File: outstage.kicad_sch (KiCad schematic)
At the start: 4 parts, among them M3001 Fan, M3002 Fan

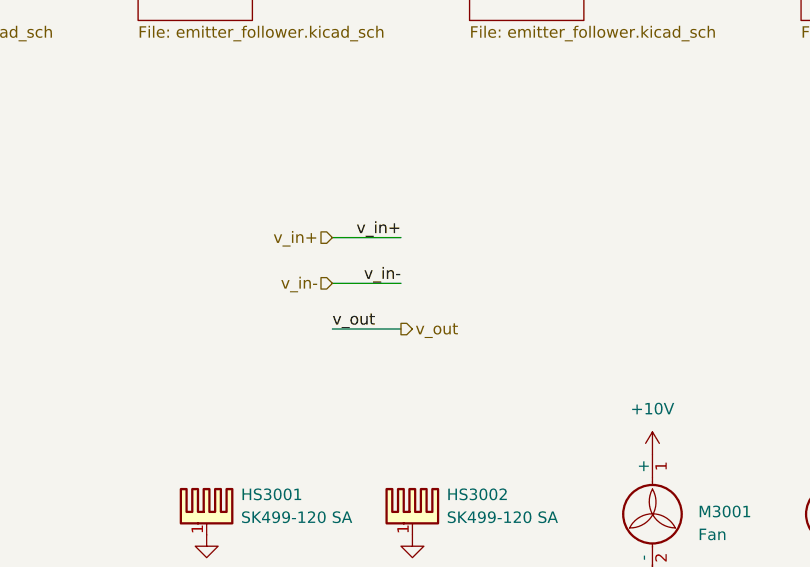
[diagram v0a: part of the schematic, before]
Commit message: add pss 3dmodels and testpoints
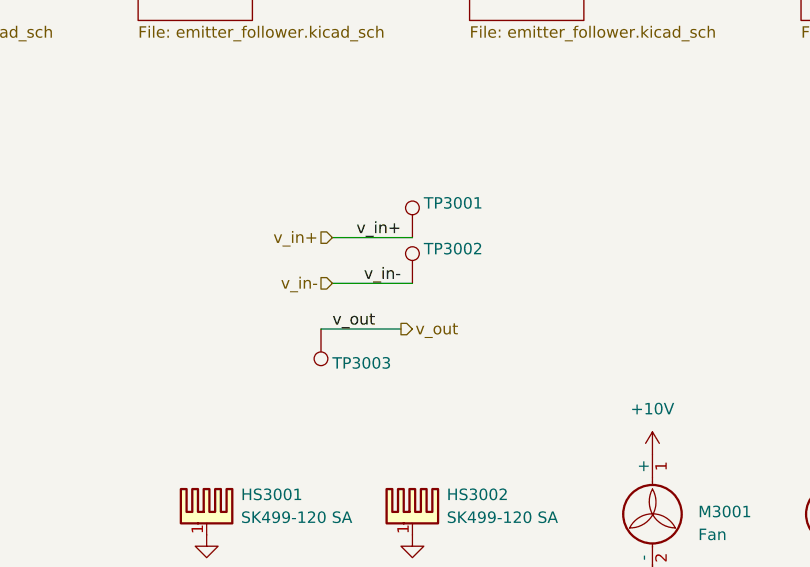
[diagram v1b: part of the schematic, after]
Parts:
- added TP3001, TP3002, TP3003: ~, pss:TP_0805_2012Metric, symbol Connector:TestPoint
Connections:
- net v_in+: now also TP3001.1
- net v_in-: now also TP3002.1
- net v_out: now also TP3003.1

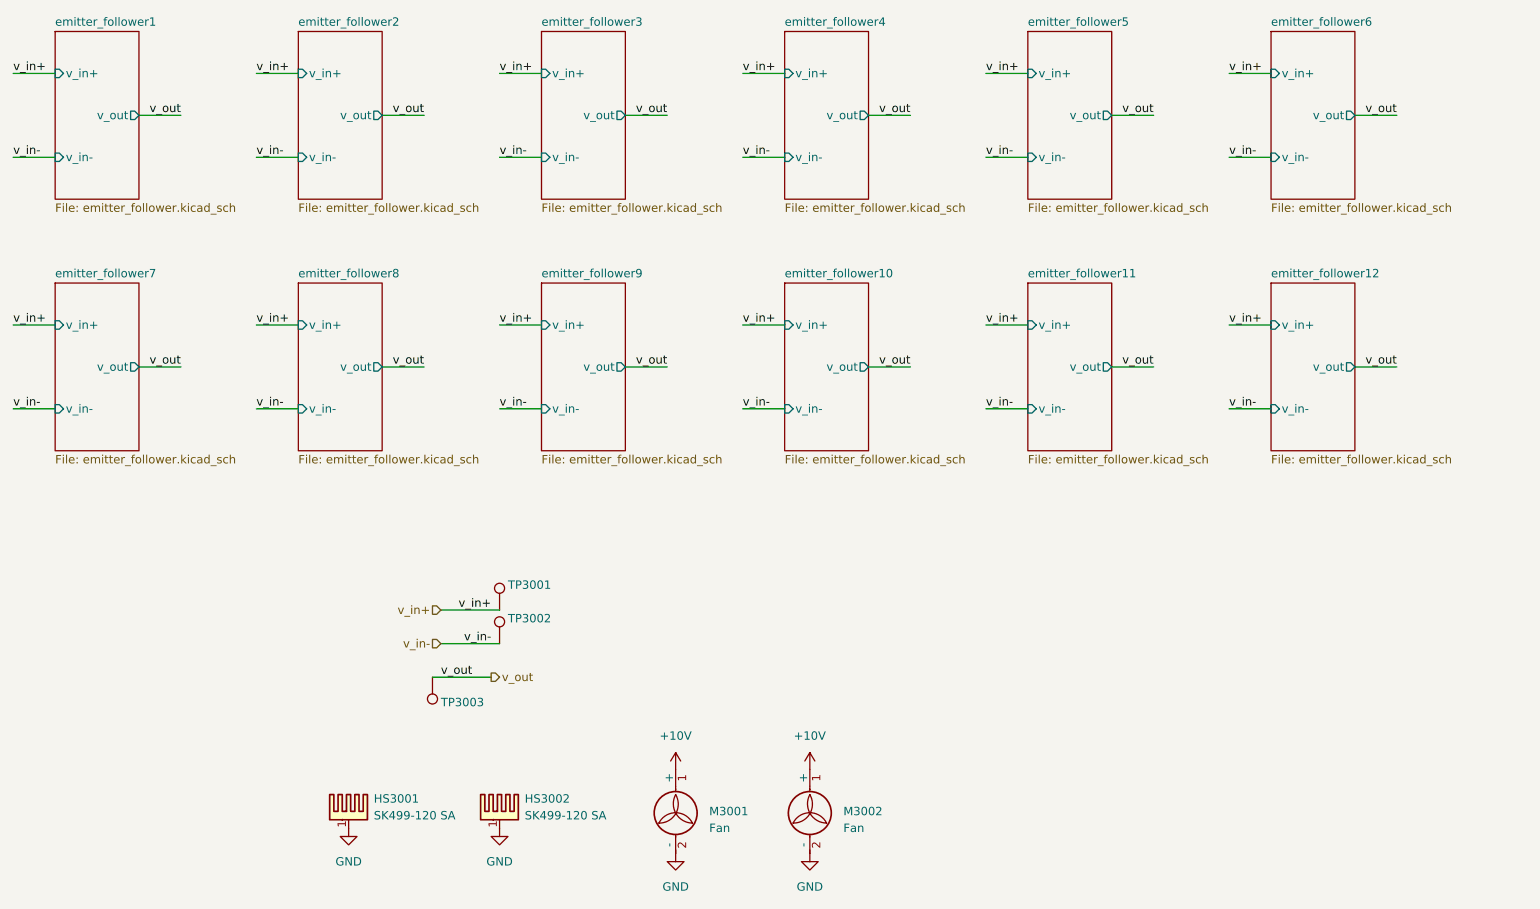
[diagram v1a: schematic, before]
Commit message: add outstage separation by connectors for individual PCB
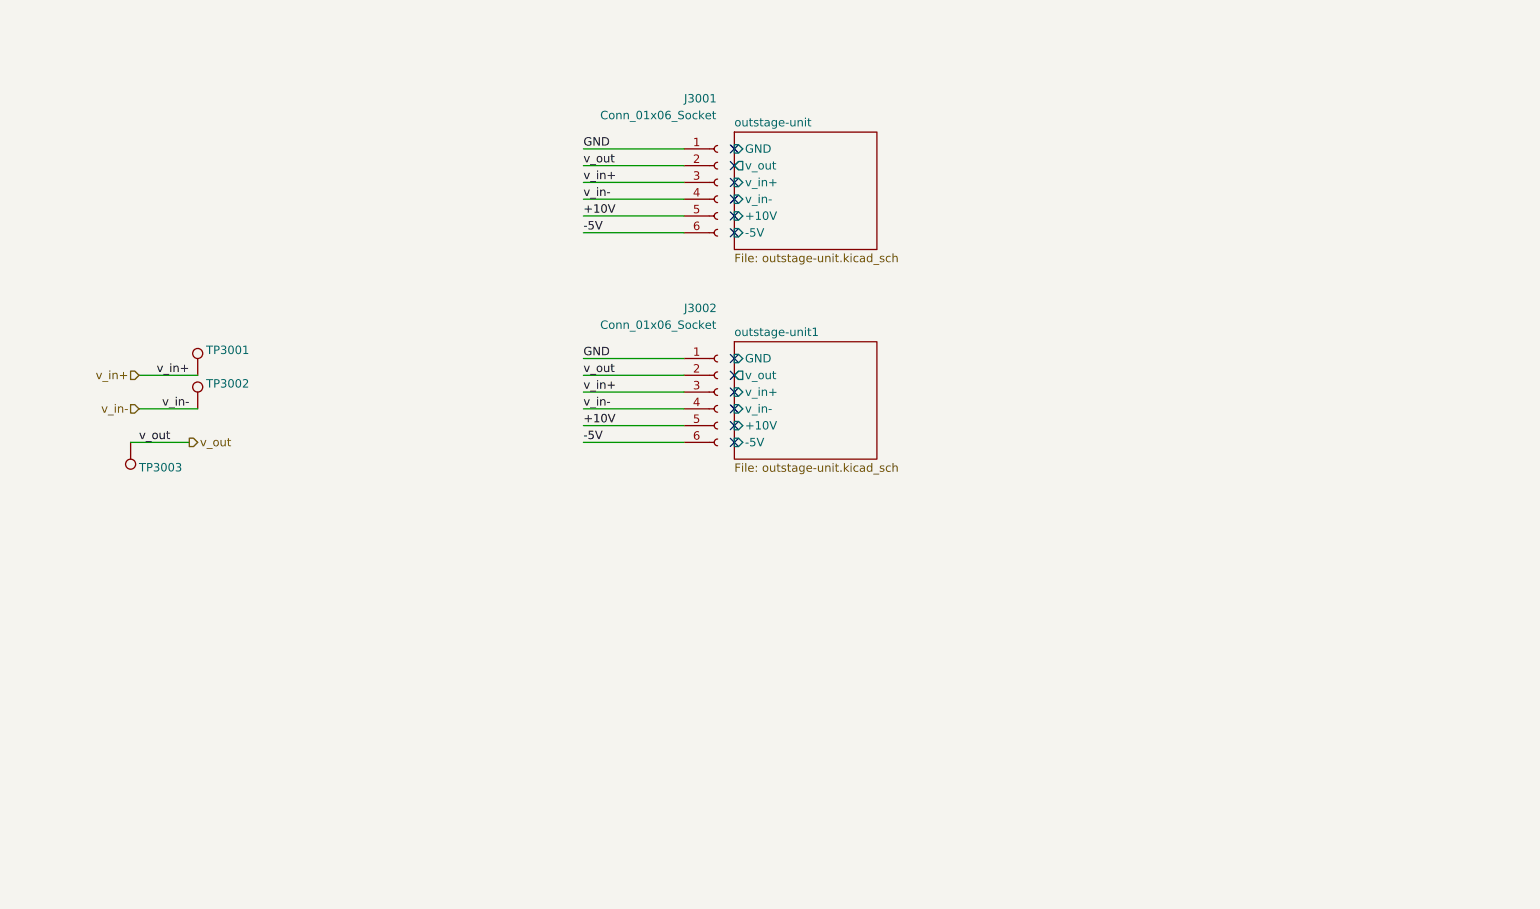
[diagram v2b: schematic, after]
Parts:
- removed HS3001, HS3002: SK499-120 SA, pss:Heatsink_Fischer_SK499-120_46x120mm_h33mm_Drill3.5mm_ScrewM3, symbol pss:Heatsink_Pad
- removed M3001, M3002: Fan, pss:Fan_SameSky_CFM-5015V, symbol pss:Fan
- added J3001, J3002: Conn_01x06_Socket, pss:PhoenixContact_TDPT_2,5_6-SP-5,08_1x06_P5.08mm_Horizontal, symbol Connector:Conn_01x06_Socket
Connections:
- net +10V: now also J3001.5 (Pin_5), J3002.5 (Pin_5)
- net GND: now also J3001.1 (Pin_1), J3002.1 (Pin_1)
- net v_in+: now also J3001.3 (Pin_3), J3002.3 (Pin_3)
- net v_in-: now also J3001.4 (Pin_4), J3002.4 (Pin_4)
- net v_out: now also J3001.2 (Pin_2), J3002.2 (Pin_2)
- new net -5V: J3001.6 (Pin_6), J3002.6 (Pin_6)
- no-connect marks 0 -> 12
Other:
- removed sheet emitter_follower1
- removed sheet emitter_follower10
- removed sheet emitter_follower11
- removed sheet emitter_follower12
- removed sheet emitter_follower2
- removed sheet emitter_follower3
- removed sheet emitter_follower4
- removed sheet emitter_follower5
- removed sheet emitter_follower6
- removed sheet emitter_follower7
- removed sheet emitter_follower8
- removed sheet emitter_follower9
- added sheet outstage-unit (outstage-unit.kicad_sch)
- added sheet outstage-unit1 (outstage-unit.kicad_sch)
- moved on the sheet: TP3001, TP3002, TP3003

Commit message: add bias separate power supply net
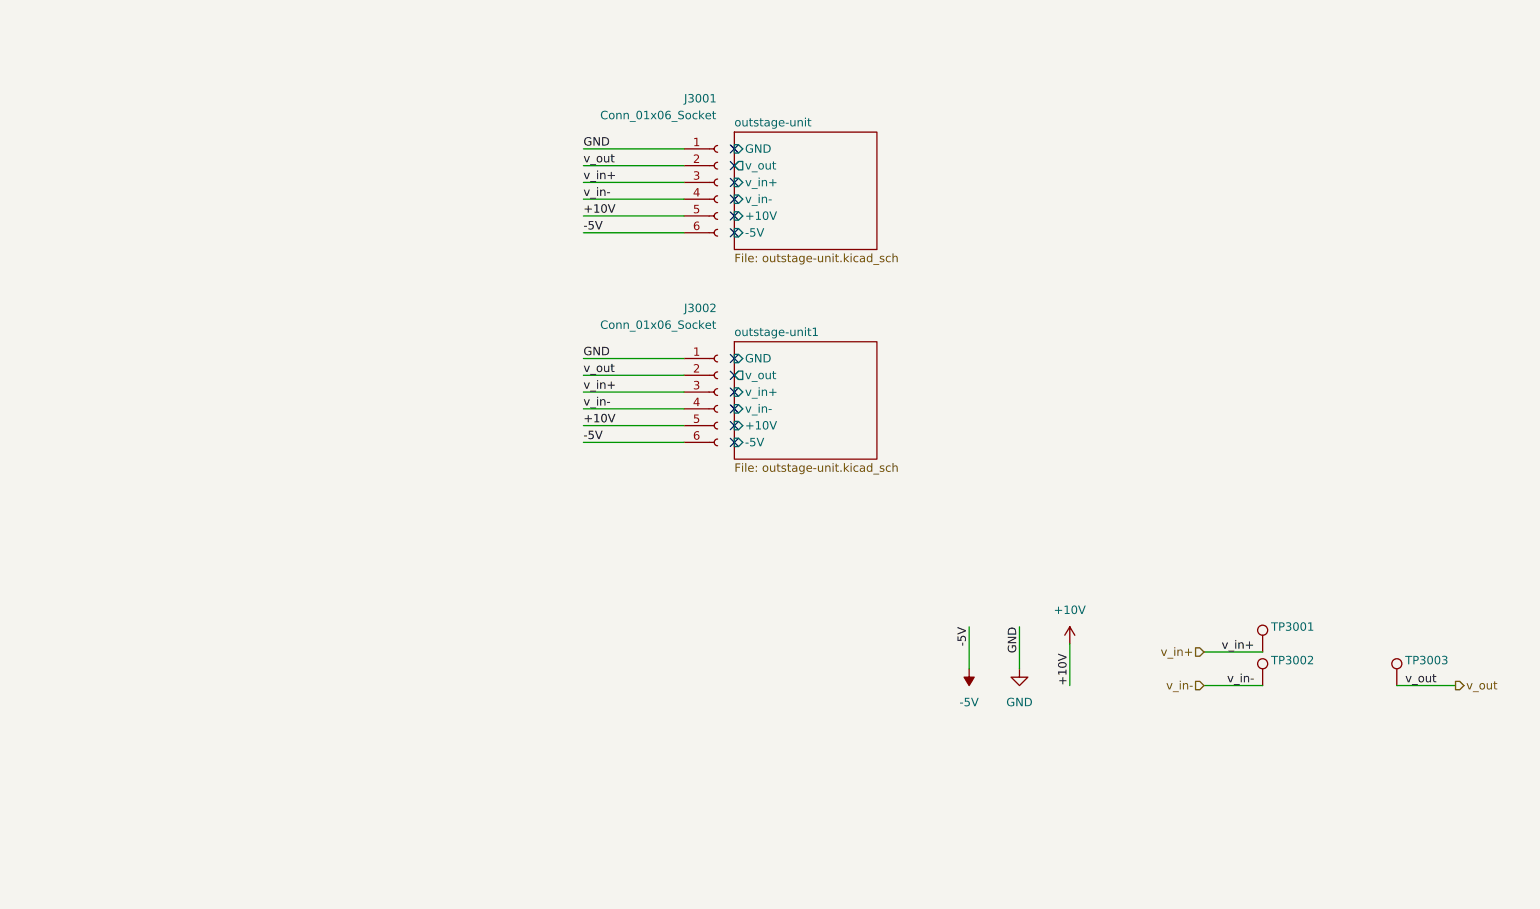
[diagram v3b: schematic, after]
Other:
- moved on the sheet: TP3001, TP3002, TP3003

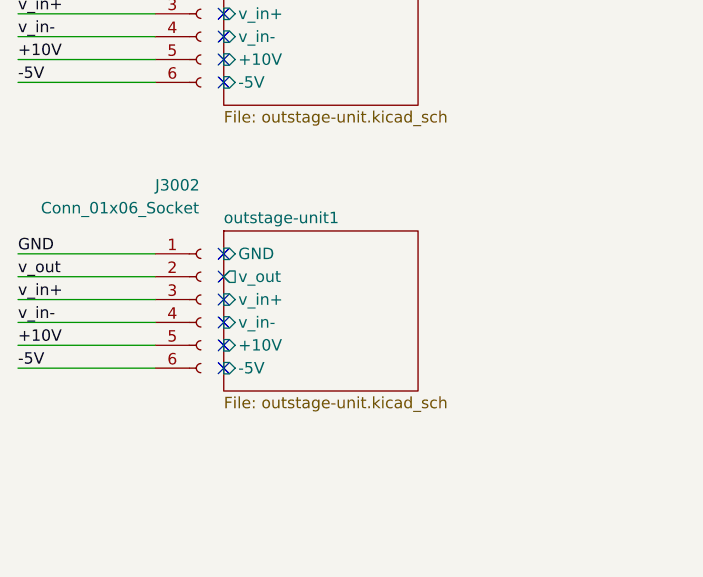
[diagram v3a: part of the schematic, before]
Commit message: edit pss alphabetically order pages
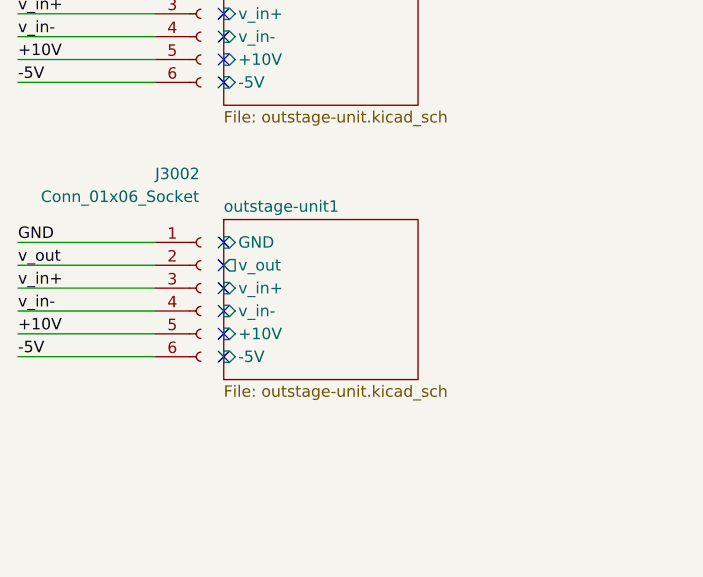
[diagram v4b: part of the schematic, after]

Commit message: edit pss symbol library: export all schematic symbols to library 'pss' and update symbol link
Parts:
- J3001, J3002: symbol Connector:Conn_01x06_Socket -> pss:Conn_01x06_Socket
- TP3001, TP3002, TP3003: symbol Connector:TestPoint -> pss:TestPoint
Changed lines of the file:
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@@
 	)
 	(symbol
-		(lib_id "Connector:TestPoint")
+		(lib_id "pss:TestPoint")
 		(at 248.92 158.75 0)
 		(unit 1)
@@
 	)
 	(symbol
-		(lib_id "Connector:TestPoint")
+		(lib_id "pss:TestPoint")
 		(at 228.6 158.75 0)
 		(unit 1)
@@
 	)
 	(symbol
-		(lib_id "Connector:Conn_01x06_Socket")
+		(lib_id "pss:Conn_01x06_Socket")
 		(at 146.05 82.55 0)
 		(unit 1)
@@
 	)
 	(symbol
-		(lib_id "Connector:Conn_01x06_Socket")
+		(lib_id "pss:Conn_01x06_Socket")
 		(at 146.05 113.03 0)
 		(unit 1)
@@
 	)
 	(symbol
-		(lib_id "Connector:TestPoint")
+		(lib_id "pss:TestPoint")
 		(at 228.6 153.67 0)
 		(unit 1)

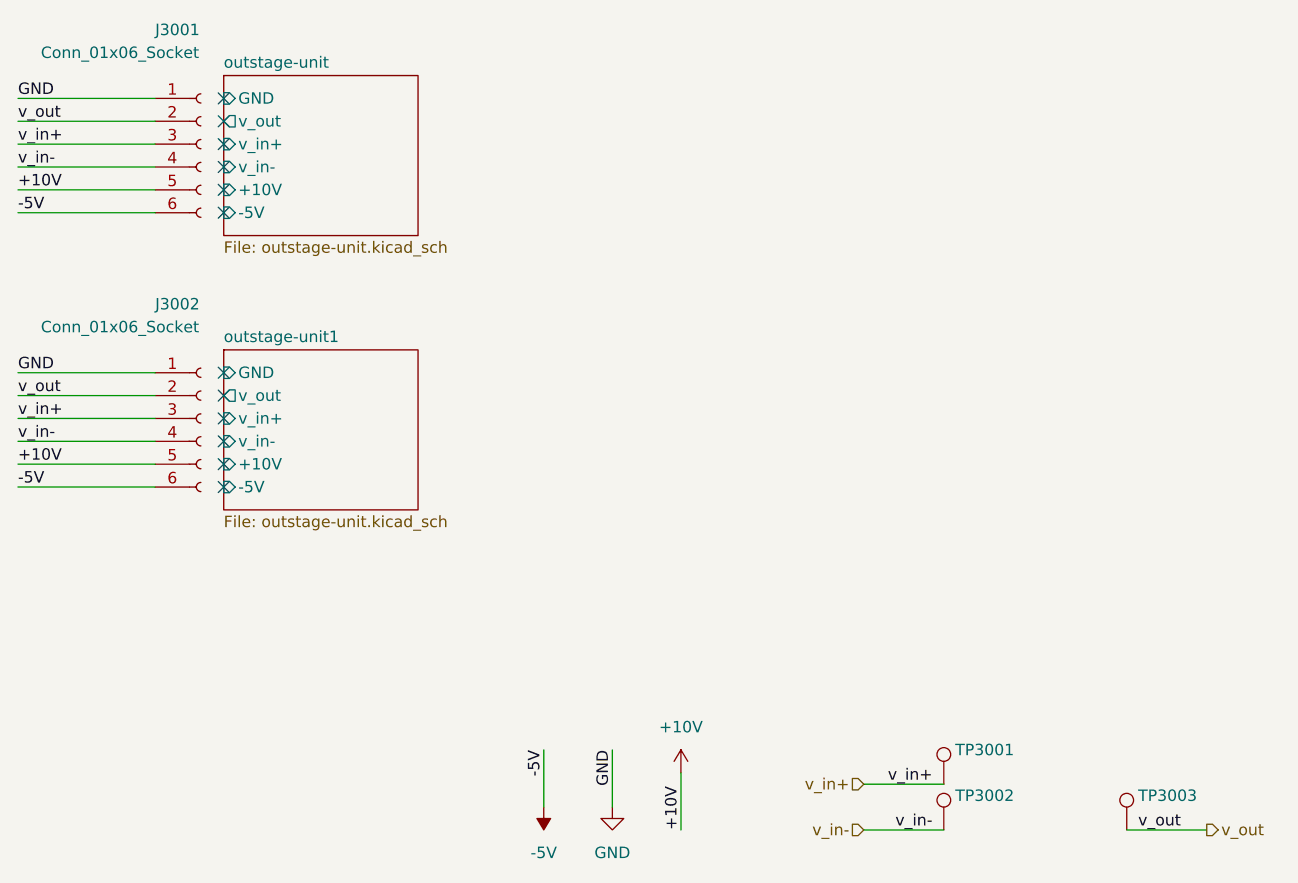
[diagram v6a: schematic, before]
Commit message: edit pss footprint library: export all footprints to library 'pss' and update footprint links
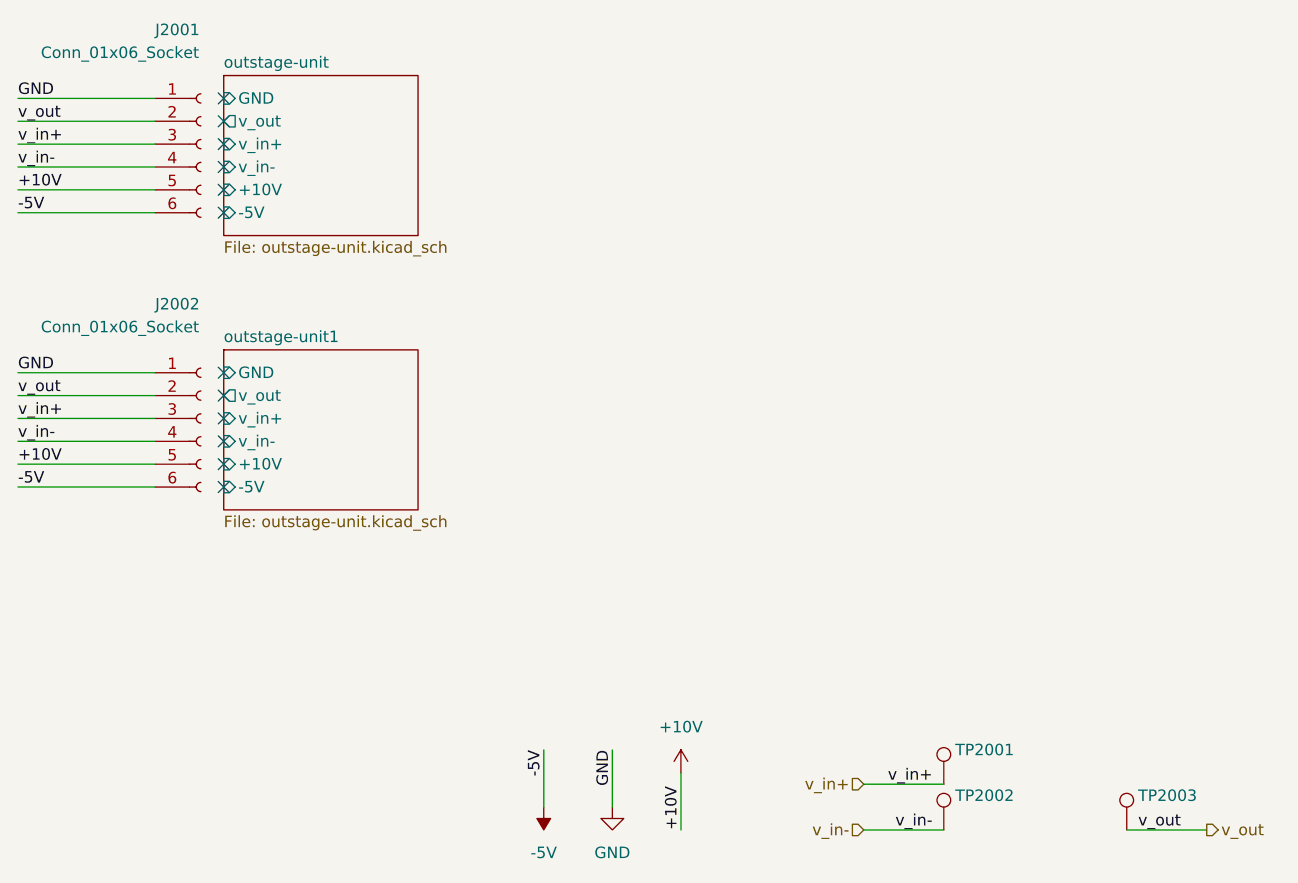
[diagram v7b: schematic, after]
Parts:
- renumbered J3001 to J2001, J3002 to J2002, TP3001 to TP2001, TP3002 to TP2002, TP3003 to TP2003
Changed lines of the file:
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@@
 		(on_board yes)
 		(dnp no)
-		(property "Reference" "TP3003"
+		(property "Reference" "TP2003"
 			(at 250.19 154.94 0)
 			(effects
@@
 		(dnp no)
 		(fields_autoplaced yes)
-		(property "Reference" "#PWR03002"
+		(property "Reference" "#PWR02001"
 			(at 184.15 152.4 0)
 			(effects
@@
 		(on_board yes)
 		(dnp no)
-		(property "Reference" "TP3002"
+		(property "Reference" "TP2002"
 			(at 229.87 154.94 0)
 			(effects
@@
 		(on_board yes)
 		(dnp no)
-		(property "Reference" "J3001"
+		(property "Reference" "J2001"
 			(at 140.97 69.85 0)
 			(effects
@@
 		(dnp no)
 		(fields_autoplaced yes)
-		(property "Reference" "#PWR03003"
+		(property "Reference" "#PWR02003"
 			(at 199.39 156.21 0)
 			(effects
@@
 		(dnp no)
 		(fields_autoplaced yes)
-		(property "Reference" "#PWR03001"
+		(property "Reference" "#PWR02002"
 			(at 191.77 162.56 0)
 			(effects
@@
 		(on_board yes)
 		(dnp no)
-		(property "Reference" "J3002"
+		(property "Reference" "J2002"
 			(at 140.97 100.33 0)
 			(effects
@@
 		(on_board yes)
 		(dnp no)
-		(property "Reference" "TP3001"
+		(property "Reference" "TP2001"
 			(at 229.87 149.86 0)
 			(effects
